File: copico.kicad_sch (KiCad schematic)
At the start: 53 parts, among them P1 CocoEdgeConnector, P10 Power Bus, P2 5V Data Bus, P3 3.3V Data Bus, P4 3.3V Address Bus, P5 Debug, U1 74LS133, U2 74LS06, U3 PicoW, U4 SN74LVC245A, U5 SN74LVC4245A, U6 SN74LVC245A, U7 SN74LVC245A, U8 SN74LVC245A, U9 74LS138

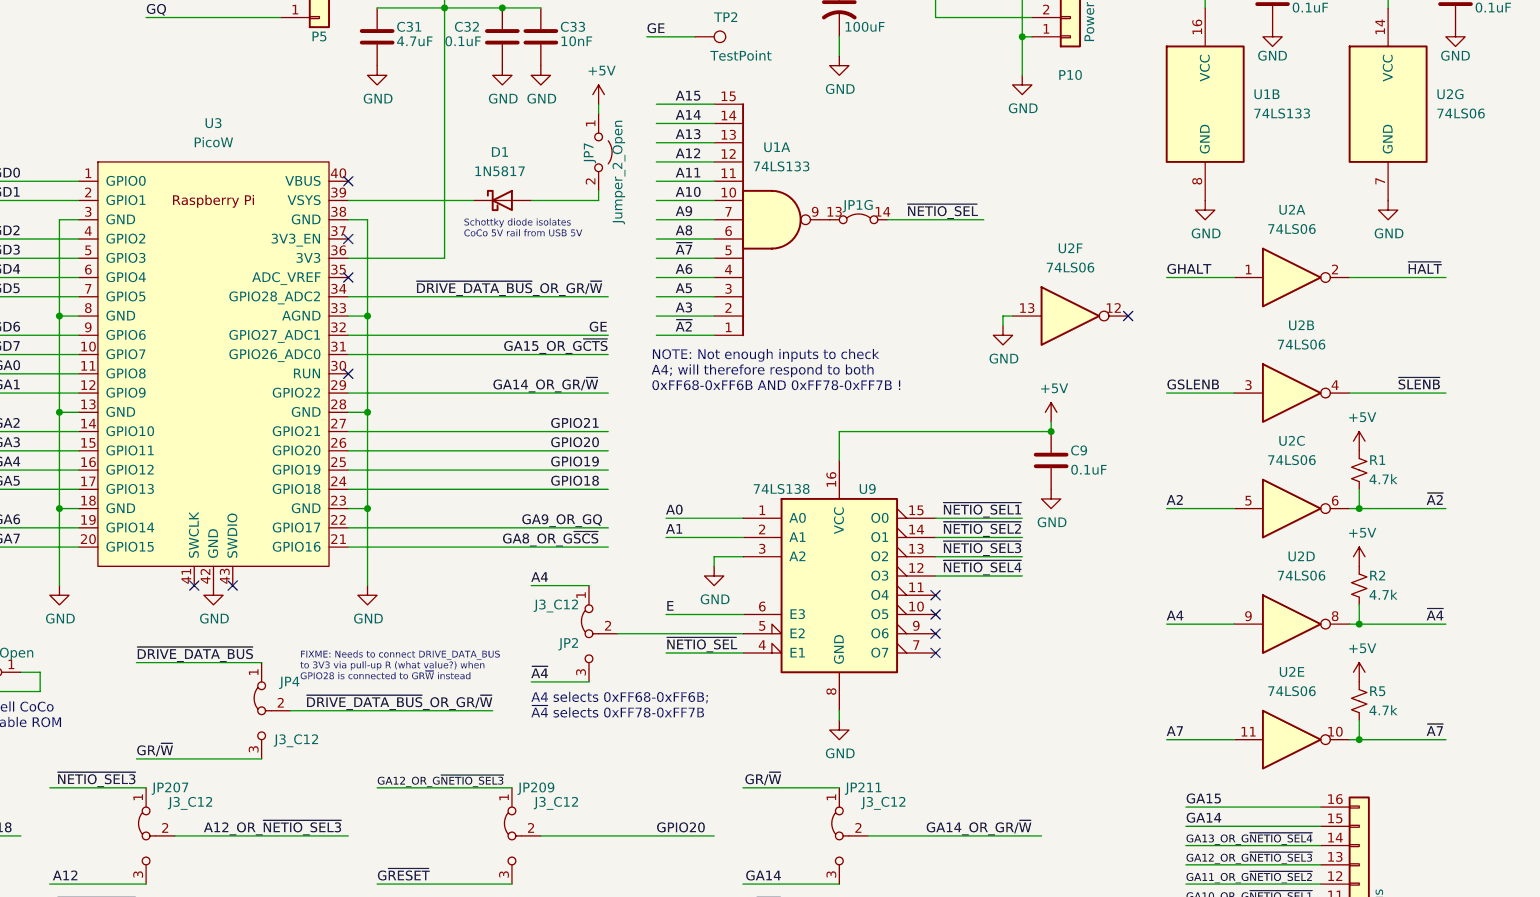
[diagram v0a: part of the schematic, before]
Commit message: Assigned Nets, added pullup for drive_data_bus
Assigned Netclasses for PWR, GND, and Addresses(3.3V only).

Added pullup resistor to drive_data_bus when jumper changed to
disconnected from pi

Added 4pin series jumper with custom symbol to connect the
pullup resistor.
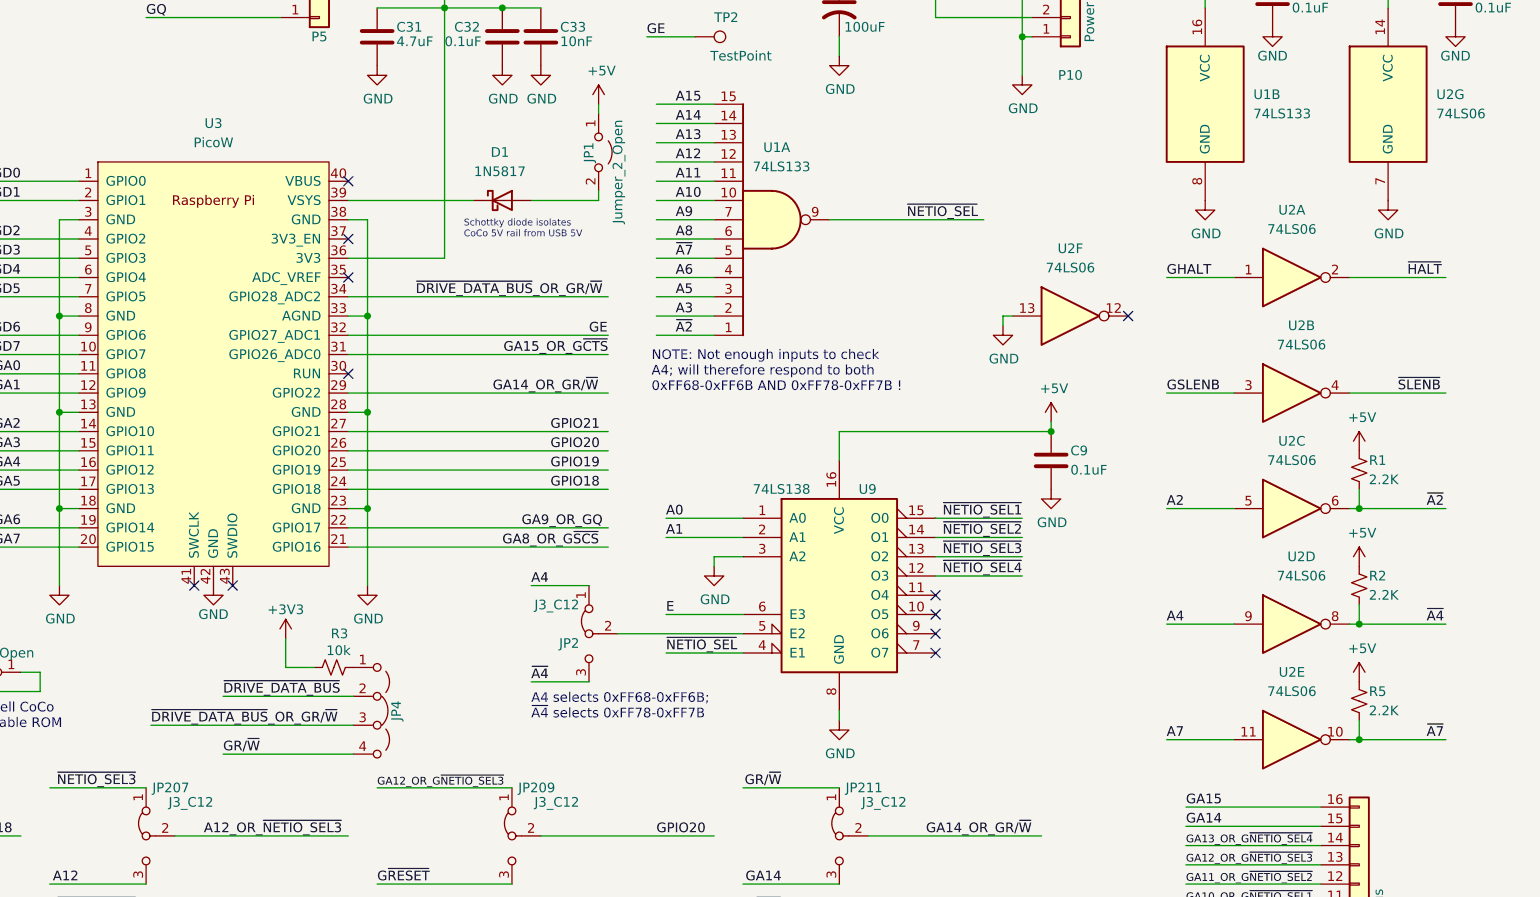
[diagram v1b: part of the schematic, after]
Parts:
- removed JP1: 8JP2NC, Connector_PinHeader_2.54mm:PinHeader_2x08_P2.54mm_Vertical, symbol Octal_Jumper_2_Bridged:Octal_Jumper_2_Bridged
- removed JP4: J3_C12, Connector_PinHeader_2.54mm:PinHeader_1x03_P2.54mm_Vertical, symbol Jumper:Jumper_3_Bridged12
- added JP4: jp_ser_4pin_23cl, Connector_PinHeader_2.54mm:PinHeader_1x04_P2.54mm_Vertical, symbol Nix_Symbols:jp_ser_4pin_23cl
- added R3: 10k, Resistor_THT:R_Axial_DIN0207_L6.3mm_D2.5mm_P10.16mm_Horizontal, symbol Device:R_Small_US
- C31: footprint PCM_Capacitor_THT_US_AKL:CP_Radial_Tantal_D4.5mm_P5.00mm -> Capacitor_THT:C_Rect_L4.0mm_W2.5mm_P2.50mm
- JP1: renamed from JP7; footprint (none) -> Connector_PinHeader_2.54mm:PinHeader_1x02_P2.54mm_Vertical
- JP10, JP11, JP12, JP3: footprint (none) -> Connector_PinHeader_2.54mm:PinHeader_1x02_P2.54mm_Vertical
- P5: footprint Connector_PinHeader_2.54mm:PinHeader_1x04_P2.54mm_Vertical -> Connector_PinHeader_2.54mm:PinHeader_1x05_P2.54mm_Vertical
- R1, R2, R5: value 4.7k -> 2.2K
- TP1, TP2: footprint (none) -> Connector_PinHeader_2.54mm:PinHeader_1x01_P2.54mm_Vertical
- U9: footprint (none) -> Package_DIP:DIP-16_W7.62mm_LongPads
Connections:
- net +3V3: now also R3.1
- net GR/~{W}: now also JP4.4 (D)
- net ~{DRIVE_DATA_BUS}: now also JP4.2 (B)
- net ~{DRIVE_DATA_BUS}_OR_GR/~{W}: now also JP4.3 (C)
- net ~{NETIO_SEL}: now also U1.9
- new net: JP4.1 (A), R3.2
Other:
- note removed: "FIXME: Needs to connect DRIVE_DATA_BUS to 3V3 via pull-up R (what value?) when GPIO28 is connected to GR~{W} instead"

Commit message: Changed some capacitors and labels
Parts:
- removed C31: 4.7uF, Capacitor_THT:C_Rect_L4.0mm_W2.5mm_P2.50mm, symbol Device:C
- removed C33: 10nF, Capacitor_THT:C_Disc_D5.0mm_W2.5mm_P5.00mm, symbol Device:C
- removed JP1: Jumper_2_Open, Connector_PinHeader_2.54mm:PinHeader_1x02_P2.54mm_Vertical, symbol Jumper:Jumper_2_Open
- added C35, C4: 0.1uF, Capacitor_THT:C_Disc_D5.0mm_W2.5mm_P5.00mm, symbol Device:C
- added JP5: Jumper_2_Open, Connector_PinHeader_2.54mm:PinHeader_1x02_P2.54mm_Vertical, symbol Jumper:Jumper_2_Open
- renumbered C32 to C33, C73 to C53, C75 to C55, C4 to C6, C5 to C7, JP201 to JP101, JP202 to JP102, JP203 to JP103, JP204 to JP104, JP205 to JP105, JP206 to JP106, JP207 to JP107, JP208 to JP108, JP209 to JP109, JP210 to JP110, JP211 to JP111, JP212 to JP112, R5 to R3, R3 to R4
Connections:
- net +3V3: now also C4.2
- net +5V: now also JP5.1 (A)
- net GND: now also C35.2, C4.1
- net at D1.1 (K), U3.39 (VSYS): now also C35.1
- net at D1.2 (A): now also JP5.2 (B)
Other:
- note added: "NOTE: Only one of U4 or U5 should be installed."
- note removed: "NOTE: C73 will be placed near VCC of both U6 and U7"
- note removed: "NOTE: Only one of U4 or U5 should be installed; they have overlapping footprints on the PCB."
- moved on the sheet: C33, TP1, TP2
